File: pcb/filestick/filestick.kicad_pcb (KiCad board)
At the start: 4 copper layers, 106 parts, among them J1 USB_B_Micro, J2 DIN-5_180degree, J3 DIN-5_180degree, J4 Micro_SD_Card_Det2, J5 Conn_01x08_Pin, J6 Conn_01x09_Pin, J7 Conn_01x02_Pin, J8 Conn_02x08_Odd_Even, J9 Conn_01x02_Pin, Q1 2N7002, Q2 2N7002, Q3 2N7002, Q4 2N7002, Q5 2N7002, U1 ICE40UP5K-SG48ITR, U2 FT230XS, U3 SN65HVD75, U4 SN65HVD75, U5 AT25SF081-SSHD-X, U6 LD1117S33TR_SOT223, U7 LD1117S12TR_SOT223, U8 LMV324, X1 ASV-xxxMHz

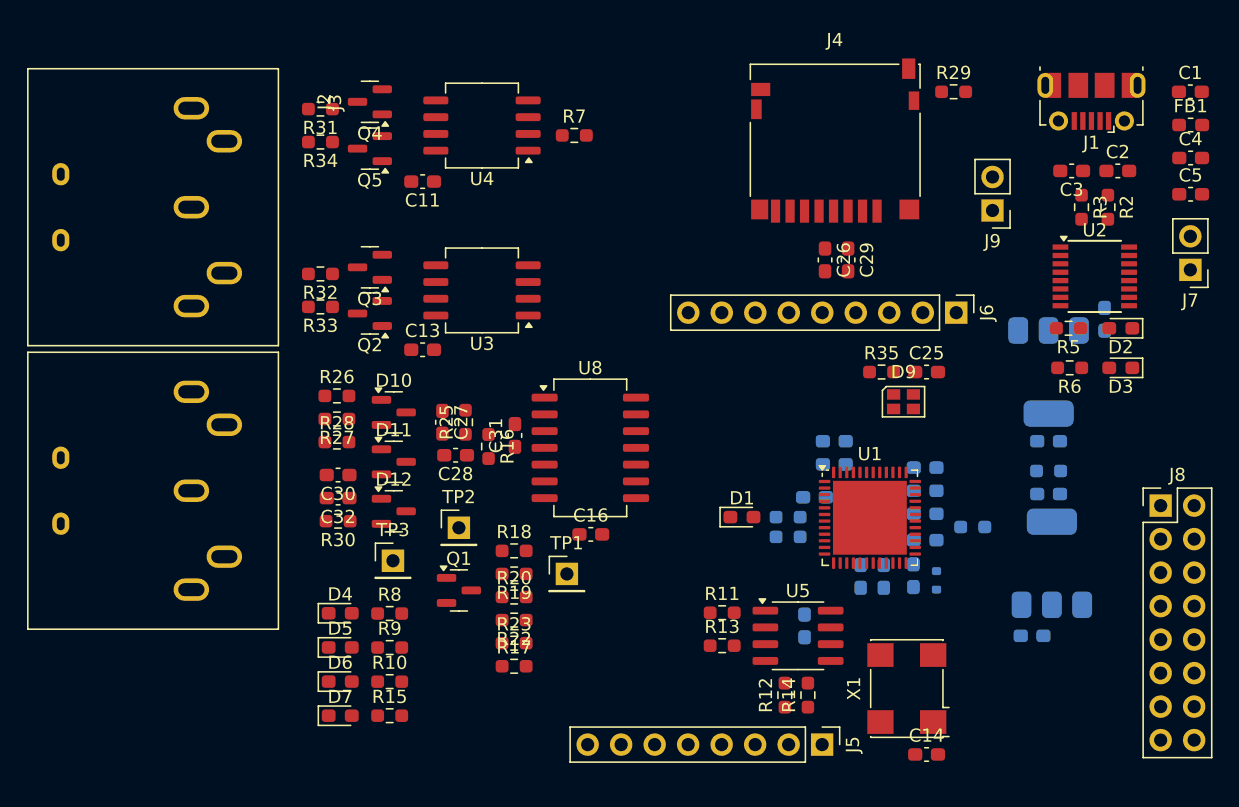
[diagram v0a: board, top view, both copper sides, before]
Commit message: Fix econet socket on schematic and route econet front end
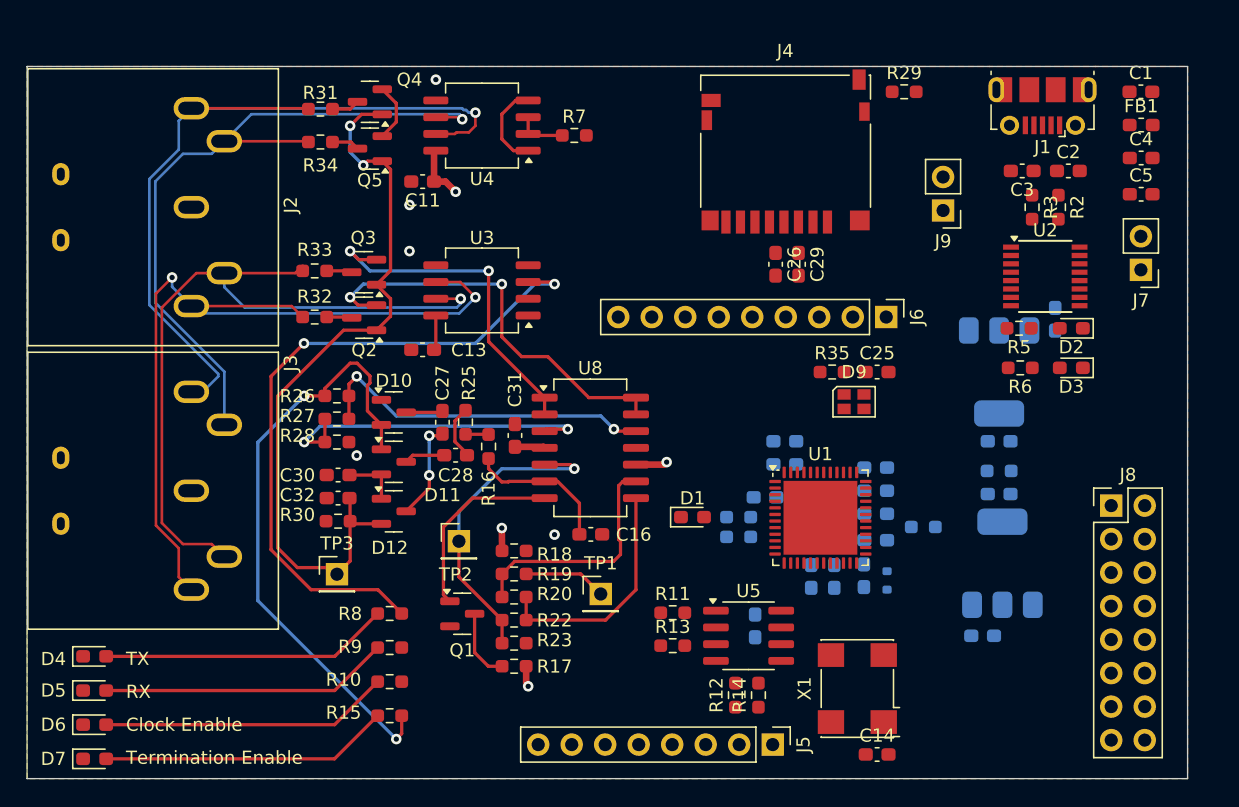
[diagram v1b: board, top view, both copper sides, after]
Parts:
- moved D4 18.9 mm to (106.6, 121.2)
- moved D5 18.9 mm to (106.6, 123.8)
- moved D6 18.9 mm to (106.6, 126.4)
- moved D7 18.9 mm to (106.6, 129.0)
- moved J6 5.32 mm to (166.7, 95.5)
- moved TP3 4.37 mm to (125.0, 115.0)
- moved J4 3.85 mm to (159.0, 83.0)
- moved Q3 3.84 mm to (127.1, 95.5)
- moved C29 3.77 mm to (160.0, 91.5)
- moved C26 3.76 mm to (158.3, 91.5)
- moved C1 3.75 mm to (186.0, 78.4)
- moved C10 3.75 mm to (159.0, 106.7)
- moved C12 3.75 mm to (159.0, 104.9)
- moved C14 3.75 mm to (166.0, 128.7)
- moved C15 3.75 mm to (156.7, 118.9)
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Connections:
- J3 pad 1: /DATA- -> /DATA+
- J3 pad 4: /DATA+ -> /DATA-
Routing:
- net /DATA+: track 0.00 -> 62.6 mm, vias 0 -> 2
- net /CLK-: track 0.00 -> 61.2 mm, vias 0 -> 1
- net /TERM_EN_9V: track 0.00 -> 57.2 mm, vias 0 -> 2
- net /DATA-: track 0.00 -> 56.1 mm, vias 0 -> 1
- net /CLK+: track 0.00 -> 54.7 mm, vias 0 -> 1
- net /ECONET_TX_ENABLE: track 0.00 -> 51.5 mm, vias 0 -> 2
- net /ECONET_TERM_EN: track 0.00 -> 46.6 mm, vias 0 -> 2
- net /TERM_HI: track 0.00 -> 31.5 mm, vias 0 -> 2
- net /V_1V8: track 0.00 -> 26.4 mm, vias 0 -> 2
- net /TERM_LO: track 0.00 -> 26.0 mm, vias 0 -> 2
- net /V_1V4: track 0.00 -> 25.7 mm, vias 0 -> 2
- net /COLLISION_MON: track 0.00 -> 24.8 mm, vias 0 -> 1
- net Net-(D7-A): track 0.00 -> 21.9 mm
- net Net-(D6-A): track 0.00 -> 21.9 mm
- net Net-(D5-A): track 0.00 -> 21.9 mm
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- added copper zone on In2.Cu, net +3V3
- added copper zone on F.Cu, net GND
- added copper zone on In1.Cu, net GND
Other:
- board outline added: 88 x 54 mm
- board text added: "Clock Enable"
- board text added: "RX"
- board text added: "TX"
- board text added: "Termination Enable"

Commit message: Improve fpga pin assignments
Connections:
- J8 pad 1: /GPIO_6 -> /GPIO_37
- J8 pad 10: /GPIO_26 -> /GPIO_25
- J8 pad 11: /GPIO_37 -> /GPIO_23
- J8 pad 12: /GPIO_44 -> /GPIO_21
- J8 pad 2: /GPIO_9 -> /GPIO_36
- J8 pad 3: /GPIO_10 -> /GPIO_35
- J8 pad 4: /GPIO_11 -> /GPIO_34
- J8 pad 5: /GPIO_12 -> /GPIO_32
- J8 pad 6: /GPIO_13 -> /GPIO_31
- J8 pad 7: /GPIO_18 -> /GPIO_28
- J8 pad 8: /GPIO_19 -> /GPIO_27
- J8 pad 9: /GPIO_21 -> /GPIO_26
- U1 pad 10: /GPIO_10 -> /ECONET_TX_ENABLE
- U1 pad 11: /GPIO_11 -> /ECONET_RX
- U1 pad 12: /GPIO_12 -> /ECONET_TERM_EN
- U1 pad 13: /GPIO_13 -> /COLLISION_REF_PWM
- U1 pad 18: /GPIO_18 -> /COLLISION_DETECT
- U1 pad 19: /GPIO_19 -> /ECONET_RECEIVING
- U1 pad 23: /UART_TX -> /GPIO_23
- U1 pad 25: /UART_RX -> /GPIO_25
- U1 pad 27: /ECONET_RECEIVING -> /GPIO_27
- U1 pad 28: /ECONET_TERM_EN -> /GPIO_28
- U1 pad 31: /COLLISION_REF_PWM -> /GPIO_31
- U1 pad 32: /COLLISION_DETECT -> /GPIO_32
- U1 pad 34: /ECONET_CLKIO -> /GPIO_34
- U1 pad 35: /ECONET_CLKIO -> /GPIO_35
- U1 pad 36: /ECONET_TX -> /GPIO_36
- U1 pad 38: /ECONET_CLKEN -> /UART_RX
- U1 pad 42: /ECONET_TX_ENABLE -> /UART_TX
- U1 pad 43: /ECONET_RX -> /ECONET_CLKIO
- U1 pad 44: /GPIO_44 -> /ECONET_CLKIO
- U1 pad 6: /GPIO_6 -> /ECONET_CLKEN
- U1 pad 9: /GPIO_9 -> /ECONET_TX
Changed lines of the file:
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@@
 	(net 52 "/UART_CBUS3")
 	(net 53 "/UART_CBUS0")
-	(net 54 "/GPIO_13")
-	(net 55 "/GPIO_18")
-	(net 56 "/GPIO_19")
-	(net 57 "/GPIO_12")
+	(net 54 "/GPIO_31")
+	(net 55 "/GPIO_28")
+	(net 56 "/GPIO_27")
+	(net 57 "/GPIO_32")
 	(net 58 "/GPIO_21")
 	(net 59 "/GPIO_37")
-	(net 60 "/GPIO_11")
-	(net 61 "/GPIO_10")
-	(net 62 "/GPIO_9")
-	(net 63 "/GPIO_6")
-	(net 64 "/GPIO_44")
+	(net 60 "/GPIO_23")
+	(net 61 "/GPIO_34")
+	(net 62 "/GPIO_35")
+	(net 63 "/GPIO_36")
+	(net 64 "/GPIO_25")
 	(net 65 "/GPIO_26")
 	(net 66 "/UART_CTS")
@@
 		(tags "resistor handsolder")
 		(property "Reference" "R9"
-			(at 2.9975 0.063333 360)
+			(at 2.9975 0.063333 0)
 			(layer "F.SilkS")
 			(effects
@@
 		)
 		(property "Value" "560"
-			(at 0 1.43 360)
+			(at 0 1.43 0)
 			(layer "F.Fab")
 			(effects
@@
 		)
 		(fp_text user "${REFERENCE}"
-			(at 0 0 360)
+			(at 0 0 0)
 			(layer "F.Fab")
 			(effects
@@
 		(tags "resistor handsolder")
 		(property "Reference" "R8"
-			(at 2.9975 -0.02 360)
+			(at 2.9975 -0.02 0)
 			(layer "F.SilkS")
 			(effects
@@
 		)
 		(property "Value" "560"
-			(at 0 1.43 360)
+			(at 0 1.43 0)
 			(layer "F.Fab")
 			(effects
@@
 		)
 		(fp_text user "${REFERENCE}"
-			(at 0 0 360)
+			(at 0 0 0)
 			(layer "F.Fab")
 			(effects
@@
 		(tags "resistor handsolder")
 		(property "Reference" "R34"
-			(at 0 1.77 360)
+			(at 0 1.77 0)
 			(layer "F.SilkS")
 			(effects
@@
 		)
 		(property "Value" "56"
-			(at 0 1.43 360)
+			(at 0 1.43 0)
 			(layer "F.Fab")
 			(effects
@@
 		)
 		(fp_text user "${REFERENCE}"
-			(at 0 0 360)
+			(at 0 0 0)
 			(layer "F.Fab")
 			(effects
@@
 		(tags "resistor handsolder")
 		(property "Reference" "R10"
-			(at 3.4975 0.146666 360)
+			(at 3.4975 0.146666 0)
 			(layer "F.SilkS")
 			(effects
@@
 		)
 		(property "Value" "560"
-			(at 0 1.43 360)
+			(at 0 1.43 0)
 			(layer "F.Fab")
 			(effects
@@
 		)
 		(fp_text user "${REFERENCE}"
-			(at 0 0 360)
+			(at 0 0 0)
 			(layer "F.Fab")
 			(effects
@@
 		(tags "resistor handsolder")
 		(property "Reference" "R17"
-			(at -3.065 -0.02 360)
+			(at -3.065 -0.02 0)
 			(layer "F.SilkS")
 			(effects
@@
 		)
 		(property "Value" "1k"
-			(at 0 1.43 360)
+			(at 0 1.43 0)
 			(layer "F.Fab")
 			(effects
@@
 		)
 		(fp_text user "${REFERENCE}"
-			(at 0 0 360)
+			(at 0 0 0)
 			(layer "F.Fab")
 			(effects
@@
 		(tags "resistor handsolder")
 		(property "Reference" "R15"
-			(at 3.4975 0.23 360)
+			(at 3.4975 0.23 0)
 			(layer "F.SilkS")
 			(effects
@@
 		)
 		(property "Value" "560"
-			(at 0 1.43 360)
+			(at 0 1.43 0)
 			(layer "F.Fab")
 			(effects
@@
 		)
 		(fp_text user "${REFERENCE}"
-			(at 0 0 360)
+			(at 0 0 0)
 			(layer "F.Fab")
 			(effects
@@
 			(layers "F.Cu" "F.Paste" "F.Mask")
 			(roundrect_rratio 0.25)
-			(net 63 "/GPIO_6")
+			(net 79 "/ECONET_CLKEN")
 			(pinfunction "IOB_13b")
 			(pintype "bidirectional")
@@
 			(layers "F.Cu" "F.Paste" "F.Mask")
 			(roundrect_rratio 0.25)
-			(net 62 "/GPIO_9")
+			(net 95 "/ECONET_TX")
 			(pinfunction "IOB_16a")
 			(pintype "bidirectional")
@@
 			(layers "F.Cu" "F.Paste" "F.Mask")
 			(roundrect_rratio 0.25)
-			(net 61 "/GPIO_10")
+			(net 80 "/ECONET_TX_ENABLE")
 			(pinfunction "IOB_18a")
 			(pintype "bidirectional")
@@
 			(layers "F.Cu" "F.Paste" "F.Mask")
 			(roundrect_rratio 0.25)
-			(net 60 "/GPIO_11")
+			(net 93 "/ECONET_RX")
 			(pinfunction "IOB_20a")
 			(pintype "bidirectional")
@@
 			(layers "F.Cu" "F.Paste" "F.Mask")
 			(roundrect_rratio 0.25)
-			(net 57 "/GPIO_12")
+			(net 30 "/ECONET_TERM_EN")
 			(pinfunction "IOB_22a")
 			(pintype "bidirectional")
@@
 			(layers "F.Cu" "F.Paste" "F.Mask")
 			(roundrect_rratio 0.25)
-			(net 54 "/GPIO_13")
+			(net 84 "/COLLISION_REF_PWM")
 			(pinfunction "IOB_24a")
 			(pintype "bidirectional")
@@
 			(layers "F.Cu" "F.Paste" "F.Mask")
 			(roundrect_rratio 0.25)
-			(net 55 "/GPIO_18")
+			(net 68 "/COLLISION_DETECT")
 			(pinfunction "IOB_31b")
 			(pintype "bidirectional")
@@
 			(layers "F.Cu" "F.Paste" "F.Mask")
 			(roundrect_rratio 0.25)
-			(net 56 "/GPIO_19")
+			(net 81 "/ECONET_RECEIVING")
 			(pinfunction "IOB_29b")
 			(pintype "bidirectional")
@@
 			(layers "F.Cu" "F.Paste" "F.Mask")
 			(roundrect_rratio 0.25)
-			(net 94 "/UART_TX")
+			(net 60 "/GPIO_23")
 			(pinfunction "IOT_37a")
 			(pintype "bidirectional")
@@
 			(layers "F.Cu" "F.Paste" "F.Mask")
 			(roundrect_rratio 0.25)
-			(net 92 "/UART_RX")
+			(net 64 "/GPIO_25")
 			(pinfunction "IOT_36b")
 			(pintype "bidirectional")
@@
 			(layers "F.Cu" "F.Paste" "F.Mask")
 			(roundrect_rratio 0.25)
-			(net 81 "/ECONET_RECEIVING")
+			(net 56 "/GPIO_27")
 			(pinfunction "IOT_38b")
 			(pintype "bidirectional")
@@
 			(layers "F.Cu" "F.Paste" "F.Mask")
 			(roundrect_rratio 0.25)
-			(net 30 "/ECONET_TERM_EN")
+			(net 55 "/GPIO_28")
 			(pinfunction "IOT_41a")
 			(pintype "bidirectional")
@@
 			(layers "F.Cu" "F.Paste" "F.Mask")
 			(roundrect_rratio 0.25)
-			(net 84 "/COLLISION_REF_PWM")
+			(net 54 "/GPIO_31")
 			(pinfunction "IOT_42b")
 			(pintype "bidirectional")
@@
 			(layers "F.Cu" "F.Paste" "F.Mask")
 			(roundrect_rratio 0.25)
-			(net 68 "/COLLISION_DETECT")
+			(net 57 "/GPIO_32")
 			(pinfunction "IOT_43a")
 			(pintype "bidirectional")
@@
 			(layers "F.Cu" "F.Paste" "F.Mask")
 			(roundrect_rratio 0.25)
-			(net 91 "/ECONET_CLKIO")
+			(net 61 "/GPIO_34")
 			(pinfunction "IOT_44b")
 			(pintype "bidirectional")
@@
 			(layers "F.Cu" "F.Paste" "F.Mask")
 			(roundrect_rratio 0.25)
-			(net 91 "/ECONET_CLKIO")
+			(net 62 "/GPIO_35")
 			(pinfunction "IOT_46b_G0")
 			(pintype "bidirectional")
@@
 			(layers "F.Cu" "F.Paste" "F.Mask")
 			(roundrect_rratio 0.25)
-			(net 95 "/ECONET_TX")
+			(net 63 "/GPIO_36")
 			(pinfunction "IOT_48b")
 			(pintype "bidirectional")
@@
 			(layers "F.Cu" "F.Paste" "F.Mask")
 			(roundrect_rratio 0.25)
-			(net 79 "/ECONET_CLKEN")
+			(net 92 "/UART_RX")
 			(pinfunction "IOT_50b")
 			(pintype "bidirectional")
@@
 			(layers "F.Cu" "F.Paste" "F.Mask")
 			(roundrect_rratio 0.25)
-			(net 80 "/ECONET_TX_ENABLE")
+			(net 94 "/UART_TX")
 			(pinfunction "IOT_51a")
 			(pintype "bidirectional")
@@
 			(layers "F.Cu" "F.Paste" "F.Mask")
 			(roundrect_rratio 0.25)
-			(net 93 "/ECONET_RX")
+			(net 91 "/ECONET_CLKIO")
 			(pinfunction "IOT_49a")
 			(pintype "bidirectional")
@@
 			(layers "F.Cu" "F.Paste" "F.Mask")
 			(roundrect_rratio 0.25)
-			(net 64 "/GPIO_44")
+			(net 91 "/ECONET_CLKIO")
 			(pinfunction "IOB_3b_G6")
 			(pintype "bidirectional")
@@
 			(layers "*.Cu" "*.Mask")
 			(remove_unused_layers no)
-			(net 63 "/GPIO_6")
+			(net 59 "/GPIO_37")
 			(pinfunction "Pin_1")
 			(pintype "passive")
@@
 			(layers "*.Cu" "*.Mask")
 			(remove_unused_layers no)
-			(net 62 "/GPIO_9")
+			(net 63 "/GPIO_36")
 			(pinfunction "Pin_2")
 			(pintype "passive")
@@
 			(layers "*.Cu" "*.Mask")
 			(remove_unused_layers no)
-			(net 61 "/GPIO_10")
+			(net 62 "/GPIO_35")
 			(pinfunction "Pin_3")
 			(pintype "passive")
@@
 			(layers "*.Cu" "*.Mask")
 			(remove_unused_layers no)
-			(net 60 "/GPIO_11")
+			(net 61 "/GPIO_34")
 			(pinfunction "Pin_4")
 			(pintype "passive")
@@
 			(layers "*.Cu" "*.Mask")
 			(remove_unused_layers no)
-			(net 57 "/GPIO_12")
+			(net 57 "/GPIO_32")
 			(pinfunction "Pin_5")
 			(pintype "passive")
@@
 			(layers "*.Cu" "*.Mask")
 			(remove_unused_layers no)
-			(net 54 "/GPIO_13")
+			(net 54 "/GPIO_31")
 			(pinfunction "Pin_6")
 			(pintype "passive")
@@
 			(layers "*.Cu" "*.Mask")
 			(remove_unused_layers no)
-			(net 55 "/GPIO_18")
+			(net 55 "/GPIO_28")
 			(pinfunction "Pin_7")
 			(pintype "passive")
@@
 			(layers "*.Cu" "*.Mask")
 			(remove_unused_layers no)
-			(net 56 "/GPIO_19")
+			(net 56 "/GPIO_27")
 			(pinfunction "Pin_8")
 			(pintype "passive")
@@
 			(layers "*.Cu" "*.Mask")
 			(remove_unused_layers no)
-			(net 58 "/GPIO_21")
+			(net 65 "/GPIO_26")
 			(pinfunction "Pin_9")
 			(pintype "passive")
@@
 			(layers "*.Cu" "*.Mask")
 			(remove_unused_layers no)
-			(net 65 "/GPIO_26")
+			(net 64 "/GPIO_25")
 			(pinfunction "Pin_10")
 			(pintype "passive")
@@
 			(layers "*.Cu" "*.Mask")
 			(remove_unused_layers no)
-			(net 59 "/GPIO_37")
+			(net 60 "/GPIO_23")
 			(pinfunction "Pin_11")
 			(pintype "passive")
@@
 			(layers "*.Cu" "*.Mask")
 			(remove_unused_layers no)
-			(net 64 "/GPIO_44")
+			(net 58 "/GPIO_21")
 			(pinfunction "Pin_12")
 			(pintype "passive")
@@
 		(tags "resistor handsolder")
 		(property "Reference" "R32"
-			(at 0 1.55 360)
+			(at 0 1.55 0)
 			(layer "F.SilkS")
 			(effects
@@
 		)
 		(property "Value" "56"
-			(at 0 1.43 360)
+			(at 0 1.43 0)
 			(layer "F.Fab")
 			(effects
@@
 		)
 		(fp_text user "${REFERENCE}"
-			(at 0 0 360)
+			(at 0 0 0)
 			(layer "F.Fab")
 			(effects
